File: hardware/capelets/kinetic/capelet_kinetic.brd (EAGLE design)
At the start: 54.6 x 40.5 mm, 13 parts, among them IC1 CAT24C256WI-GT3

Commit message: hardware: updated capelets
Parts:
- moved R5 1.27 mm to (38.2, 40.4)
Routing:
- net +3V3: track 57.8 -> 56.1 mm
- net N$3: track 8.31 -> 7.79 mm
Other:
- board text added: "SHEPHERD v1.4 CAPELET KEH"
- board text removed: "SHEPHERD v1.3 CAPELET KEH"
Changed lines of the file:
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@@
 <?xml version="1.0" encoding="utf-8"?>
 <!DOCTYPE eagle SYSTEM "eagle.dtd">
-<eagle version="9.3.2">
+<eagle version="9.4.2">
 <drawing>
 <settings>
@@
 <board>
 <plain>
-<text x="40.259" y="42.164" size="1.27" layer="25" font="vector" ratio="15">WP</text>
-<text x="6.985" y="43.18" size="1.6764" layer="25" font="vector" ratio="15">SHEPHERD v1.3 CAPELET KEH</text>
+<text x="40.894" y="40.894" size="1.27" layer="25" font="vector" ratio="15">WP</text>
+<text x="6.096" y="43.18" size="1.6764" layer="29" font="vector" ratio="15">SHEPHERD v1.4 CAPELET KEH</text>
 <dimension x1="0" y1="45.72" x2="54.61" y2="45.72" x3="27.305" y3="50.8" textsize="1.778" layer="47"/>
 <dimension x1="54.61" y1="45.72" x2="54.61" y2="5.207" x3="63.5" y3="25.4635" textsize="1.143" textratio="16" layer="47"/>
@@
 <attribute name="VALUE" x="42.1764" y="26.67" size="1.27" layer="27" rot="R270" align="top-center"/>
 </element>
-<element name="R5" library="mylib" package="RESC2012X65" value="5.6k" x="38.227" y="41.656" smashed="yes" rot="R180">
-<attribute name="NAME" x="38.227" y="40.3984" size="1.27" layer="25" font="vector" ratio="15" rot="R180" align="bottom-center"/>
-<attribute name="VALUE" x="38.227" y="43.2946" size="1.27" layer="27" rot="R180" align="top-center"/>
+<element name="R5" library="mylib" package="RESC2012X65" value="5.6k" x="38.227" y="40.386" smashed="yes" rot="R180">
+<attribute name="NAME" x="35.433" y="40.9064" size="1.27" layer="25" font="vector" ratio="15" rot="R180" align="bottom-center"/>
+<attribute name="VALUE" x="38.227" y="42.0246" size="1.27" layer="27" rot="R180" align="top-center"/>
 </element>
 <element name="X1" library="con-wago-500" library_urn="urn:adsk.eagle:library:195" package="W237-102" package3d_urn="urn:adsk.eagle:package:10688/1" value="" x="27.305" y="10.668" smashed="yes">
@@
 <via x="46.482" y="34.29" extent="1-16" drill="0.4"/>
 <via x="43.688" y="34.29" extent="1-16" drill="0.4"/>
-<via x="41.91" y="39.37" extent="1-16" drill="0.4"/>
-<via x="39.624" y="39.37" extent="1-16" drill="0.4"/>
-<via x="43.688" y="42.418" extent="1-16" drill="0.35"/>
-<via x="39.751" y="43.688" extent="1-16" drill="0.35"/>
+<via x="44.831" y="39.878" extent="1-16" drill="0.35"/>
+<via x="41.275" y="38.989" extent="1-16" drill="0.4"/>
 </signal>
 <signal name="VDD_5V">
@@
 <wire x1="40.4321" y1="36.9062" x2="40.3813" y2="36.957" width="0.4064" layer="1"/>
 <wire x1="40.386" y1="36.8601" x2="40.4321" y2="36.9062" width="0.4064" layer="1"/>
-<wire x1="37.2766" y1="41.656" x2="37.2766" y2="43.7536" width="0.4064" layer="1"/>
-<wire x1="37.2766" y1="43.7536" x2="37.973" y2="44.45" width="0.4064" layer="1"/>
-<wire x1="37.973" y1="44.45" x2="45.085" y2="44.45" width="0.4064" layer="1"/>
 <wire x1="45.085" y1="44.45" x2="45.4046" y2="44.45" width="0.4064" layer="1"/>
-<wire x1="45.4046" y1="41.91" x2="45.4046" y2="44.1304" width="0.4064" layer="1"/>
+<wire x1="45.4046" y1="41.91" x2="45.4046" y2="43.18" width="0.4064" layer="1"/>
+<wire x1="45.4046" y1="43.18" x2="45.4046" y2="44.1304" width="0.4064" layer="1"/>
 <wire x1="45.4046" y1="44.1304" x2="45.085" y2="44.45" width="0.4064" layer="1"/>
 <contactref element="U$2" pad="P9$3"/>
@@
 <wire x1="46.355" y1="25.7196" x2="46.355" y2="21.59" width="0.3048" layer="1"/>
 <wire x1="40.386" y1="34.29" x2="38.354" y2="34.29" width="0.3048" layer="1"/>
-<wire x1="37.2766" y1="35.3674" x2="37.2766" y2="41.656" width="0.3048" layer="1"/>
+<wire x1="37.2766" y1="35.3674" x2="37.2766" y2="40.386" width="0.3048" layer="1"/>
 <wire x1="38.354" y1="34.29" x2="37.2766" y2="35.3674" width="0.3048" layer="1"/>
 <wire x1="50.165" y1="21.59" x2="52.705" y2="21.59" width="0.508" layer="1"/>
+<wire x1="37.2766" y1="40.386" x2="37.2766" y2="41.2136" width="0.4064" layer="1"/>
+<wire x1="37.2766" y1="41.2136" x2="39.243" y2="43.18" width="0.4064" layer="1"/>
+<wire x1="39.243" y1="43.18" x2="45.4046" y2="43.18" width="0.4064" layer="1"/>
 </signal>
 <signal name="SDA">
@@
 <contactref element="IC1" pad="7"/>
 <contactref element="R5" pad="1"/>
-<wire x1="44.45" y1="38.735" x2="44.45" y2="36.9062" width="0.4064" layer="1"/>
-<wire x1="39.1774" y1="41.656" x2="41.529" y2="41.656" width="0.4064" layer="1"/>
-<wire x1="41.529" y1="41.656" x2="44.45" y2="38.735" width="0.4064" layer="1"/>
-<via x="41.529" y="41.656" extent="1-16" drill="0.4" alwaysstop="yes"/>
+<wire x1="39.1774" y1="40.386" x2="42.799" y2="40.386" width="0.4064" layer="1"/>
+<via x="42.799" y="40.386" extent="1-16" drill="0.4" alwaysstop="yes"/>
+<wire x1="44.45" y1="36.9062" x2="44.45" y2="38.735" width="0.4064" layer="1"/>
+<wire x1="44.45" y1="38.735" x2="42.799" y2="40.386" width="0.4064" layer="1"/>
 </signal>
 <signal name="N$5">

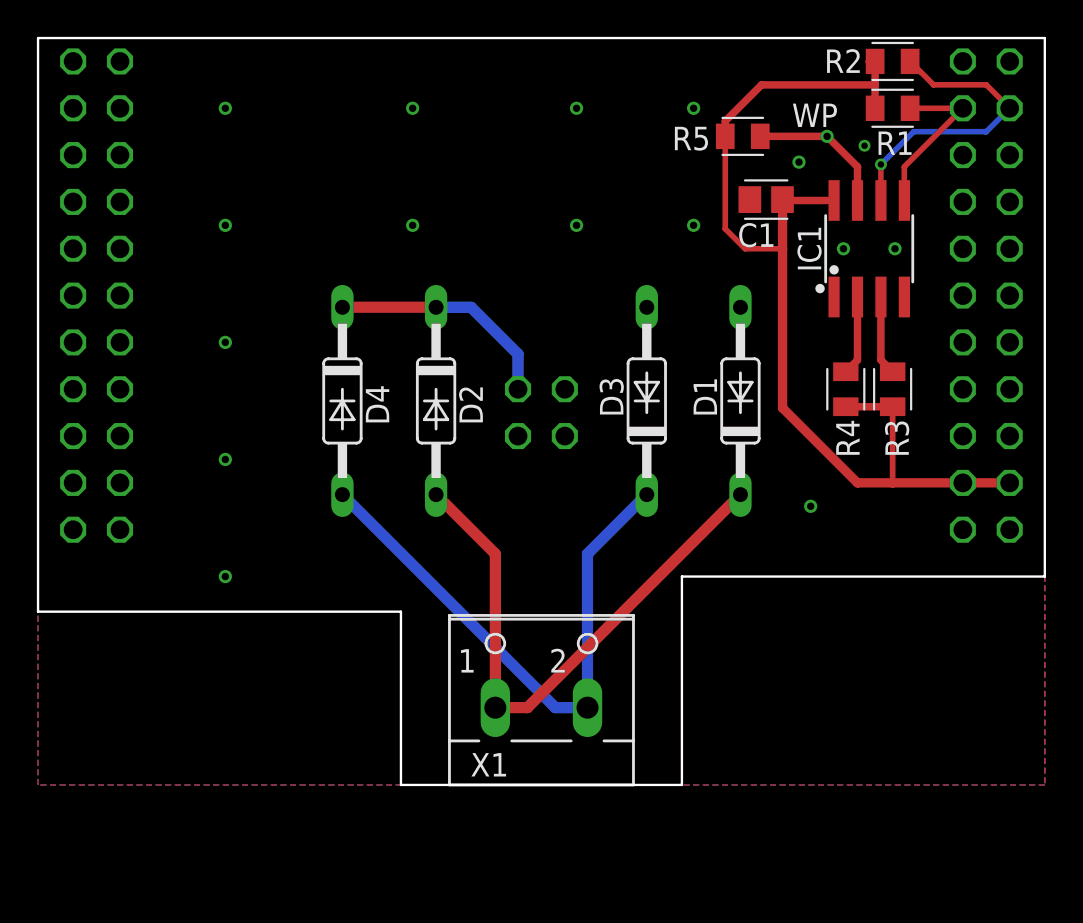
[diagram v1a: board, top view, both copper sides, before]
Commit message: hardware: prepared capelets for external manufacturing
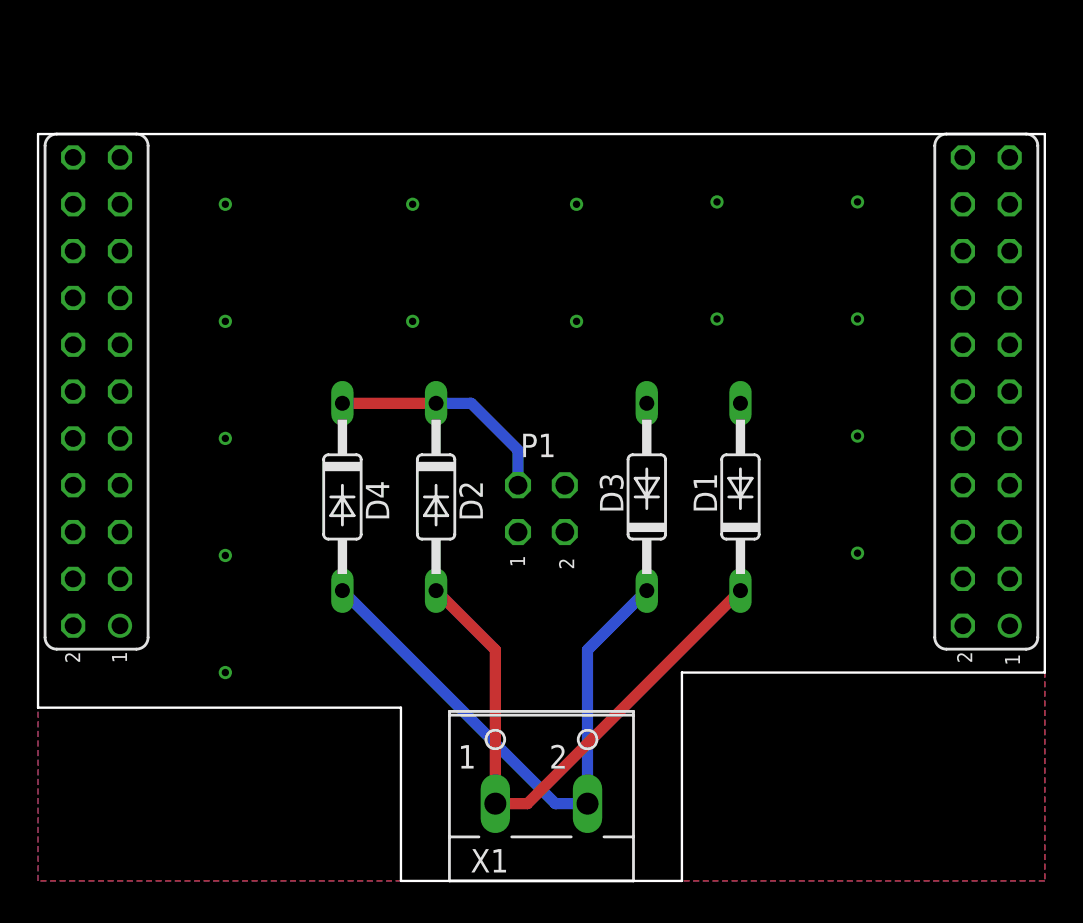
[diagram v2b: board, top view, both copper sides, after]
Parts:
- removed C1: 0.1u, mylib:CAPC2012X145
- removed IC1: CAT24C256WI-GT3, mylib:SO08
- removed R1, R2, R3, R4, R5: 5.6k, mylib:RESC2012X65
- removed U$2: SHPRD_CPLT_H, shepherd:SHPRD_CPLT_H
- added P1: (no value), pinhead:2X02
- added P8, P9: FE11-2, shepherd:FE11-2
- added U$1: (no value), shepherd:SHPRD_CPLT_H
- moved D1 5.21 mm to (38.1, 20.8)
- moved D2 5.21 mm to (21.6, 20.8)
- moved D3 5.21 mm to (33.0, 20.8)
- moved D4 5.21 mm to (16.5, 20.8)
- moved X1 5.21 mm to (27.3, 5.46)
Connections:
- removed net +3V3: C1.1, IC1.8, R1.2, R2.2, R3.2, R4.2, R5.2, U$2.P9$3, U$2.P9$4
- removed net N$3: IC1.7, R5.1
- removed net N$4: IC1.2, R4.1
- removed net N$7: IC1.3, R3.1
- removed net SCL: IC1.6, R2.1, U$2.P9$19
- removed net SDA: IC1.5, R1.1, U$2.P9$20
- removed net SYS_5V: U$2.P9$7, U$2.P9$8
- removed net VDD_5V: U$2.P9$5, U$2.P9$6
- net GND: now also P1.1, P1.2; no longer C1.2, IC1.1, IC1.4, U$2.P1$1, U$2.P1$3, U$2.P8$1, U$2.P8$2, U$2.P9$1, U$2.P9$2
- net V_H: now also P1.3; no longer U$2.P1$2
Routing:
- net +3V3: track 56.1 -> 0.00 mm
- net SCL: track 16.7 -> 0.00 mm, vias 1 -> 0
- net SDA: track 9.18 -> 0.00 mm
- net N$3: track 7.79 -> 0.00 mm, vias 1 -> 0
- net N$4: track 4.32 -> 0.00 mm
- net N$7: track 4.32 -> 0.00 mm
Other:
- board text added: "1"
- board text added: "2"
- board text added: "P1: Pins pointing to bottom, solder on top"
- board text added: "SHEPHERD v1.5 CAPELET KEH"
- board text removed: "SHEPHERD v1.4 CAPELET KEH"
- board text removed: "WP"
